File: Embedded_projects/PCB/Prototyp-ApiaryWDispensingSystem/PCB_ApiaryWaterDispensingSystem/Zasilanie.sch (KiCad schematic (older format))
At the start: 17 parts

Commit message: Many design changes have been added over the past few months #3
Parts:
- removed J?: Conn_01x02_Male, symbol Connector:Conn_01x02_Male
- added J6: Conn_02x01, Connector_PinHeader_2.54mm:PinHeader_1x02_P2.54mm_Vertical, symbol Connector_Generic:Conn_02x01
- added J?: Conn_01x02, symbol Connector_Generic:Conn_01x02
- C16, C17: footprint (none) -> Capacitor_Tantalum_SMD:CP_EIA-6032-15_Kemet-U
- C18, C19, C20, C21: footprint (none) -> Capacitor_SMD:C_0603_1608Metric
- D?: footprint (none) -> Diode_SMD:D_SMA
- D?: footprint (none) -> Diode_SMD:D_0603_1608Metric
- JP?: footprint (none) -> Jumper:SolderJumper-2_P1.3mm_Open_TrianglePad1.0x1.5mm
- R28: footprint (none) -> Resistor_SMD:R_0603_1608Metric
- U?: footprint (none) -> Package_SO:SO-8_3.9x4.9mm_P1.27mm
- gave numbers to parts that had none: 1
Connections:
- net +3V3: now also J6.1 (Pin_1)
- net GND: now also C17.2, J?.1 (Pin_1)
- net VDD: now also J6.2 (Pin_2)
- net +VDC renamed VM
- net VM: now also J?.2 (Pin_2)
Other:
- note added: "good"
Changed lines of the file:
@@
 $Descr A4 11693 8268
 encoding utf-8
-Sheet 7 9
+Sheet 6 9
 Title ""
 Date ""
@@
 F 0 "C16" H 1528 2336 50  0000 L CNN
 F 1 "10uF(25V)" H 1528 2245 50  0000 L CNN
-F 2 "" H 1448 2140 50  0001 C CNN
+F 2 "Capacitor_Tantalum_SMD:CP_EIA-6032-15_Kemet-U" H 1448 2140 50  0001 C CNN
 F 3 "~" H 1410 2290 50  0001 C CNN
 	1    1410 2290
@@
 L power:GND #PWR0208
 U 1 1 67F9830C
-P 2930 2510
-F 0 "#PWR0208" H 2930 2260 50  0001 C CNN
-F 1 "GND" H 2935 2337 50  0000 C CNN
-F 2 "" H 2930 2510 50  0001 C CNN
-F 3 "" H 2930 2510 50  0001 C CNN
-	1    2930 2510
+P 2920 2520
+F 0 "#PWR0208" H 2920 2270 50  0001 C CNN
+F 1 "GND" H 2925 2347 50  0000 C CNN
+F 2 "" H 2920 2520 50  0001 C CNN
+F 3 "" H 2920 2520 50  0001 C CNN
+	1    2920 2520
 	1    0    0    -1
 $EndComp
@@
 F 0 "C17" H 3038 2376 50  0000 L CNN
 F 1 "10uF(25V)" H 3038 2285 50  0000 L CNN
-F 2 "" H 2958 2180 50  0001 C CNN
+F 2 "Capacitor_Tantalum_SMD:CP_EIA-6032-15_Kemet-U" H 2958 2180 50  0001 C CNN
 F 3 "~" H 2920 2330 50  0001 C CNN
 	1    2920 2330
@@
 F 0 "D?" H 3100 1843 50  0000 C CNN
 F 1 "D_Small" H 3100 1934 50  0000 C CNN
-F 2 "" V 3100 2050 50  0001 C CNN
+F 2 "Diode_SMD:D_SMA" V 3100 2050 50  0001 C CNN
 F 3 "~" V 3100 2050 50  0001 C CNN
 	1    3100 2050
@@
 $EndComp
 $Comp
-L Connector:Conn_01x03_Male J?
+L Connector:Conn_01x03_Male J5
 U 1 1 67FA01B7
 P 3850 2520
-F 0 "J?" H 3958 2801 50  0000 C CNN
+F 0 "J5" H 3958 2801 50  0000 C CNN
 F 1 "Conn_01x03_Male" H 3900 2140 50  0000 C CNN
 F 2 "Connector_PinHeader_2.54mm:PinHeader_1x03_P2.54mm_Vertical" H 3850 2520 50  0001 C CNN
@@
 	1    0    0    -1
 $EndComp
-Wire Wire Line
-	2920 2180 2920 2150
-Wire Wire Line
-	2920 2150 2630 2150
-Wire Wire Line
-	2920 2150 2920 2050
-Connection ~ 2920 2150
 Connection ~ 2920 2050
 Wire Wire Line
@@
 F 0 "U?" H 3104 3886 50  0000 L CNN
 F 1 "STS7PF30L" H 3104 3795 50  0000 L CNN
-F 2 "" H 2730 3920 50  0001 C CNN
+F 2 "Package_SO:SO-8_3.9x4.9mm_P1.27mm" H 2730 3920 50  0001 C CNN
 F 3 "" H 2730 3920 50  0001 C CNN
 	1    2730 3920
@@
 F 0 "R28" H 2060 4076 50  0000 L CNN
 F 1 "4k7" H 2060 3985 50  0000 L CNN
-F 2 "" V 1920 4030 50  0001 C CNN
+F 2 "Resistor_SMD:R_0603_1608Metric" V 1920 4030 50  0001 C CNN
 F 3 "~" H 1990 4030 50  0001 C CNN
 	1    1990 4030
@@
 F 0 "C20" H 5515 3216 50  0000 L CNN
 F 1 "100n" H 5515 3125 50  0000 L CNN
-F 2 "" H 5438 3020 50  0001 C CNN
+F 2 "Capacitor_SMD:C_0603_1608Metric" H 5438 3020 50  0001 C CNN
 F 3 "~" H 5400 3170 50  0001 C CNN
 	1    5400 3170
@@
 F 0 "C21" H 5095 3066 50  0000 L CNN
 F 1 "1uF_X5R" H 5095 2975 50  0000 L CNN
-F 2 "" H 5018 2870 50  0001 C CNN
+F 2 "Capacitor_SMD:C_0603_1608Metric" H 5018 2870 50  0001 C CNN
 F 3 "~" H 4980 3020 50  0001 C CNN
 	1    4980 3020
@@
 F 0 "C18" H 6915 2996 50  0000 L CNN
 F 1 "1uF_X5R_0603" H 6220 2730 50  0000 L CNN
-F 2 "" H 6838 2800 50  0001 C CNN
+F 2 "Capacitor_SMD:C_0603_1608Metric" H 6838 2800 50  0001 C CNN
 F 3 "~" H 6800 2950 50  0001 C CNN
 	1    6800 2950
@@
 F 0 "C19" H 7315 3196 50  0000 L CNN
 F 1 "100nF" H 7315 3105 50  0000 L CNN
-F 2 "" H 7238 3000 50  0001 C CNN
+F 2 "Capacitor_SMD:C_0603_1608Metric" H 7238 3000 50  0001 C CNN
 F 3 "~" H 7200 3150 50  0001 C CNN
 	1    7200 3150
@@
 F 0 "D?" V 4579 3172 50  0000 R CNN
 F 1 "LED" V 4488 3172 50  0000 R CNN
-F 2 "" H 4540 3290 50  0001 C CNN
+F 2 "Diode_SMD:D_0603_1608Metric" H 4540 3290 50  0001 C CNN
 F 3 "~" H 4540 3290 50  0001 C CNN
 	1    4540 3290
@@
 NoConn ~ 6390 2900
 $Comp
-L Connector:Conn_01x02_Male J?
-U 1 1 67F973BC
-P 8010 2600
-F 0 "J?" H 8118 2781 50  0000 C CNN
-F 1 "Conn_01x02_Male" H 8118 2690 50  0000 C CNN
-F 2 "" H 8010 2600 50  0001 C CNN
-F 3 "~" H 8010 2600 50  0001 C CNN
-	1    8010 2600
-	1    0    0    -1
-$EndComp
-$Comp
 L power:GND #PWR0218
 U 1 1 67F9802C
@@
 	7200 2800 7200 3000
 Connection ~ 6800 2800
-$Comp
-L Jumper:Jumper_2_Open JP?
-U 1 1 67F9CBCE
-P 7600 2800
-F 0 "JP?" H 7470 2920 50  0000 C CNN
-F 1 "Jumper_2_Open" H 7560 2630 50  0000 C CNN
-F 2 "" H 7600 2800 50  0001 C CNN
-F 3 "~" H 7600 2800 50  0001 C CNN
-	1    7600 2800
-	1    0    0    -1
-$EndComp
 Wire Wire Line
 	7400 2800 7200 2800
@@
 Wire Wire Line
 	7800 2800 7870 2800
-Wire Wire Line
-	8250 2800 8250 2700
-Wire Wire Line
-	8250 2700 8210 2700
 $Comp
 L power:+3.3V #PWR0219
@@
 	7870 2760 7870 2800
 Connection ~ 7870 2800
-Wire Wire Line
-	7870 2800 8250 2800
-$Comp
-L power:VDD #PWR?
+$Comp
+L power:VDD #PWR0238
 U 1 1 6830AB4B
-P 8580 2510
-F 0 "#PWR?" H 8580 2360 50  0001 C CNN
-F 1 "VDD" H 8595 2683 50  0000 C CNN
-F 2 "" H 8580 2510 50  0001 C CNN
-F 3 "" H 8580 2510 50  0001 C CNN
-	1    8580 2510
-	1    0    0    -1
-$EndComp
-Wire Wire Line
-	8210 2600 8580 2600
-Wire Wire Line
-	8580 2600 8580 2510
-$Comp
-L power:+5VP #PWR?
+P 8955 2800
+F 0 "#PWR0238" H 8955 2650 50  0001 C CNN
+F 1 "VDD" H 8970 2973 50  0000 C CNN
+F 2 "" H 8955 2800 50  0001 C CNN
+F 3 "" H 8955 2800 50  0001 C CNN
+	1    8955 2800
+	1    0    0    -1
+$EndComp
+$Comp
+L power:+5VP #PWR0239
 U 1 1 68379F03
 P 1800 3620
-F 0 "#PWR?" H 1800 3470 50  0001 C CNN
+F 0 "#PWR0239" H 1800 3470 50  0001 C CNN
 F 1 "+5VP" H 1815 3793 50  0000 C CNN
 F 2 "" H 1800 3620 50  0001 C CNN
@@
 Wire Wire Line
 	2230 2350 2230 2650
-$Comp
-L power:+VDC #PWR?
-U 1 1 689704B4
-P 1000 1780
-F 0 "#PWR?" H 1000 1680 50  0001 C CNN
-F 1 "+VDC" H 1000 2055 50  0000 C CNN
-F 2 "" H 1000 1780 50  0001 C CNN
-F 3 "" H 1000 1780 50  0001 C CNN
-	1    1000 1780
-	1    0    0    -1
-$EndComp
-Wire Wire Line
-	1000 1780 1000 2050
+Wire Wire Line
+	2920 2050 2920 2180
+Wire Wire Line
+	2920 2480 2920 2520
+Text HLabel 1115 920  0    50   Output ~ 0
+PWR_ENn
+Text GLabel 1285 920  2    50   Output ~ 0
+PWR_ENn
+Wire Wire Line
+	1285 920  1115 920
+Text Notes 925  2375 0    50   ~ 0
+good
+$Comp
+L Jumper:Jumper_2_Open JP?
+U 1 1 67F9CBCE
+P 7600 2800
+F 0 "JP?" H 7470 2920 50  0000 C CNN
+F 1 "Jumper_2_Open" H 7560 2630 50  0000 C CNN
+F 2 "Jumper:SolderJumper-2_P1.3mm_Open_TrianglePad1.0x1.5mm" H 7600 2800 50  0001 C CNN
+F 3 "~" H 7600 2800 50  0001 C CNN
+	1    7600 2800
+	1    0    0    -1
+$EndComp
+$Comp
+L Connector_Generic:Conn_02x01 J6
+U 1 1 68EED7C1
+P 8520 2800
+F 0 "J6" H 8570 3017 50  0000 C CNN
+F 1 "Conn_02x01" H 8570 2926 50  0000 C CNN
+F 2 "Connector_PinHeader_2.54mm:PinHeader_1x02_P2.54mm_Vertical" H 8520 2800 50  0001 C CNN
+F 3 "~" H 8520 2800 50  0001 C CNN
+	1    8520 2800
+	1    0    0    -1
+$EndComp
+Wire Wire Line
+	7870 2800 8320 2800
+Wire Wire Line
+	8955 2800 8820 2800
+$Comp
+L Connector_Generic:Conn_01x02 J?
+U 1 1 68ED6183
+P 640 2150
+F 0 "J?" H 558 1825 50  0000 C CNN
+F 1 "Conn_01x02" H 558 1916 50  0000 C CNN
+F 2 "" H 640 2150 50  0001 C CNN
+F 3 "~" H 640 2150 50  0001 C CNN
+	1    640  2150
+	-1   0    0    1
+$EndComp
+Wire Wire Line
+	1000 2050 840  2050
+Connection ~ 1000 2050
+$Comp
+L power:GND #PWR?
+U 1 1 68ED818B
+P 895 2150
+F 0 "#PWR?" H 895 1900 50  0001 C CNN
+F 1 "GND" H 900 1977 50  0000 C CNN
+F 2 "" H 895 2150 50  0001 C CNN
+F 3 "" H 895 2150 50  0001 C CNN
+	1    895  2150
+	1    0    0    -1
+$EndComp
+Wire Wire Line
+	895  2150 840  2150
+Text GLabel 1285 1050 2    50   Output ~ 0
+VM
+Text HLabel 1115 1050 0    50   Output ~ 0
+VM
+Wire Wire Line
+	1285 1050 1115 1050
+Text GLabel 915  1755 0    50   Output ~ 0
+VM
+Wire Wire Line
+	915  1755 1000 1755
+Wire Wire Line
+	1000 1755 1000 2050
 $EndSCHEMATC

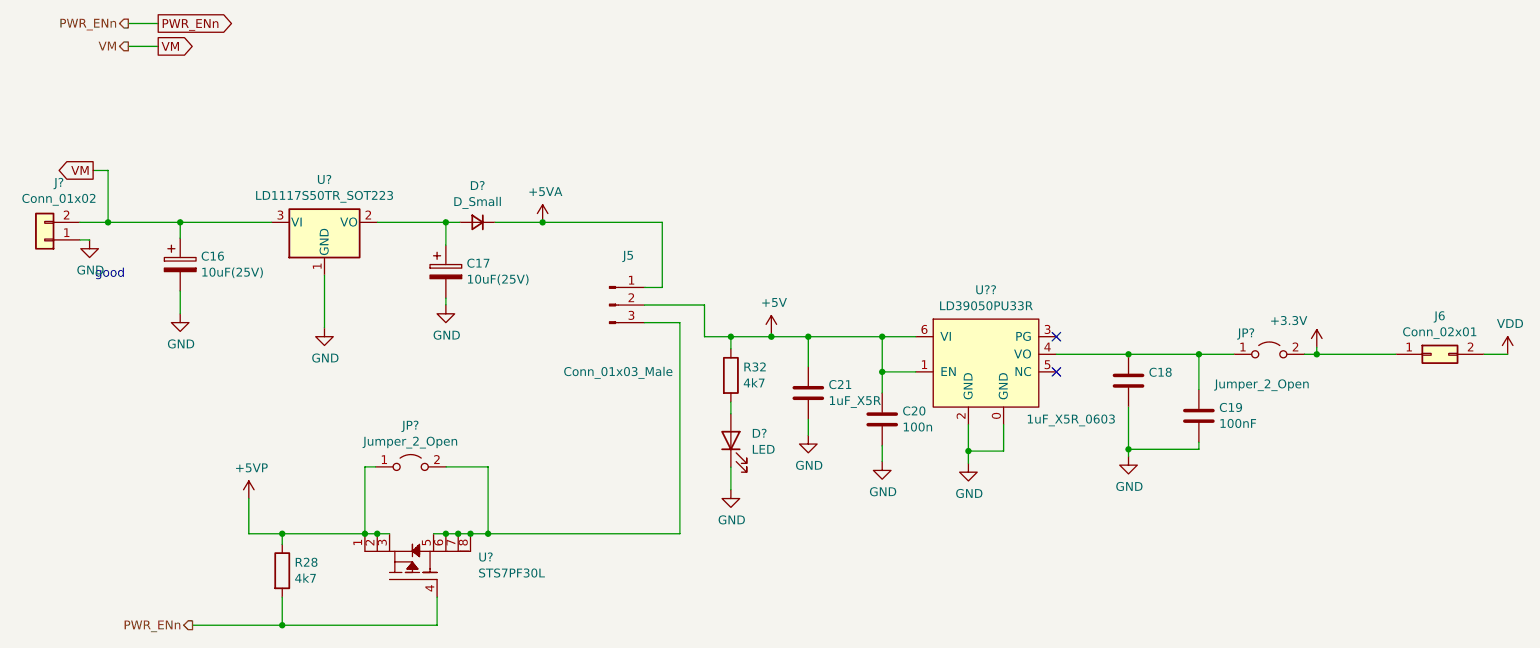
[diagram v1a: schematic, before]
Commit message: All signal has been routed, the analog part needs to be completed
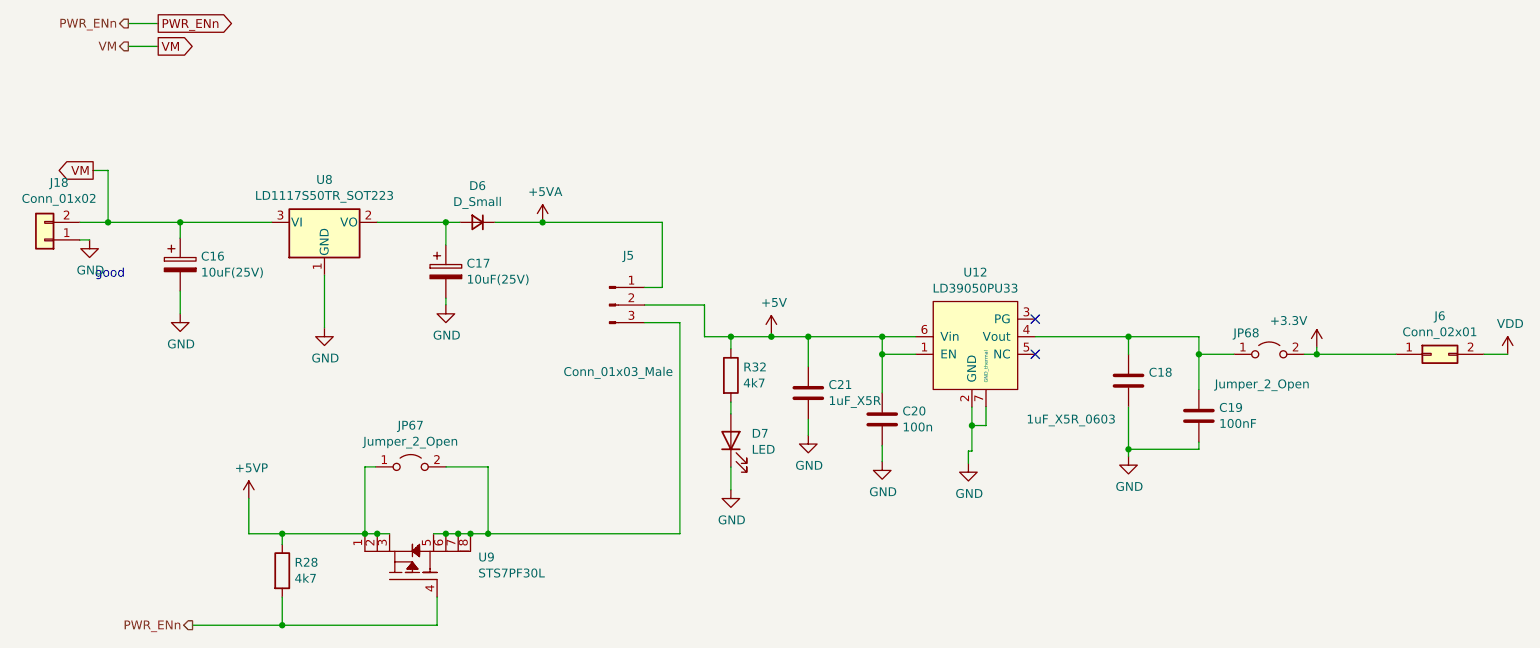
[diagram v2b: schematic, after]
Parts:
- removed U??: LD39050PU33R, symbol ApiaryWaterDispensingSystem:LD39050PU33R
- added U12: LD39050PU33, Package_SON:WSON-6-1EP_3x3mm_P0.95mm, symbol ApiaryWaterDispensingSystem:LD39050PU33
- J18: renamed from J?; footprint (none) -> TerminalBlock_4Ucon:TerminalBlock_4Ucon_1x02_P3.50mm_Vertical
- JP67: renamed from JP?; footprint (none) -> Jumper:SolderJumper-2_P1.3mm_Open_TrianglePad1.0x1.5mm
- R32: footprint (none) -> Resistor_SMD:R_0603_1608Metric
- gave numbers to parts that had none: 5
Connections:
- net +5V: now also U12.1 (EN), U12.6 (Vin)
- net GND: now also U12.2 (GND), U12.7 (GND_thermal)
- net at C18.1, C19.1, JP68.1 (A): now also U12.4 (Vout)
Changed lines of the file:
@@
 $EndDescr
-$Comp
-L ApiaryWaterDispensingSystem:LD39050PU33R U??
-U 1 1 67F96C5D
-P 5990 2800
-F 0 "U??" H 5990 3165 50  0000 C CNN
-F 1 "LD39050PU33R" H 5990 3074 50  0000 C CNN
-F 2 "" H 5990 2800 50  0001 C CNN
-F 3 "" H 5990 2800 50  0001 C CNN
-	1    5990 2800
-	1    0    0    -1
-$EndComp
 $Comp
 L Device:CP C16
@@
 $EndComp
 $Comp
-L Device:D_Small D?
+L Device:D_Small D6
 U 1 1 67F9ACDF
 P 3100 2050
-F 0 "D?" H 3100 1843 50  0000 C CNN
+F 0 "D6" H 3100 1843 50  0000 C CNN
 F 1 "D_Small" H 3100 1934 50  0000 C CNN
 F 2 "Diode_SMD:D_SMA" V 3100 2050 50  0001 C CNN
@@
 Connection ~ 4770 2700
 $Comp
-L Jumper:Jumper_2_Open JP?
+L Jumper:Jumper_2_Open JP67
 U 1 1 67FA53C3
 P 2720 3440
-F 0 "JP?" H 2720 3675 50  0000 C CNN
+F 0 "JP67" H 2720 3675 50  0000 C CNN
 F 1 "Jumper_2_Open" H 2720 3584 50  0000 C CNN
-F 2 "" H 2720 3440 50  0001 C CNN
+F 2 "Jumper:SolderJumper-2_P1.3mm_Open_TrianglePad1.0x1.5mm" H 2720 3440 50  0001 C CNN
 F 3 "~" H 2720 3440 50  0001 C CNN
 	1    2720 3440
@@
 $EndComp
 $Comp
-L ApiaryWaterDispensingSystem:STS7PF30L U?
+L ApiaryWaterDispensingSystem:STS7PF30L U9
 U 1 1 67FAB112
 P 2730 3920
-F 0 "U?" H 3104 3886 50  0000 L CNN
+F 0 "U9" H 3104 3886 50  0000 L CNN
 F 1 "STS7PF30L" H 3104 3795 50  0000 L CNN
 F 2 "Package_SO:SO-8_3.9x4.9mm_P1.27mm" H 2730 3920 50  0001 C CNN
@@
 F 0 "R32" H 4610 2966 50  0000 L CNN
 F 1 "4k7" H 4610 2875 50  0000 L CNN
-F 2 "" V 4470 2920 50  0001 C CNN
+F 2 "Resistor_SMD:R_0603_1608Metric" V 4470 2920 50  0001 C CNN
 F 3 "~" H 4540 2920 50  0001 C CNN
 	1    4540 2920
@@
 $EndComp
 $Comp
-L Device:LED D?
+L Device:LED D7
 U 1 1 67FB2F5D
 P 4540 3290
-F 0 "D?" V 4579 3172 50  0000 R CNN
+F 0 "D7" V 4579 3172 50  0000 R CNN
 F 1 "LED" V 4488 3172 50  0000 R CNN
 F 2 "Diode_SMD:D_0603_1608Metric" H 4540 3290 50  0001 C CNN
@@
 Wire Wire Line
 	5400 3410 5400 3320
-Wire Wire Line
-	5590 2900 5400 2900
-Wire Wire Line
-	5400 2900 5400 3020
-Wire Wire Line
-	5400 2900 5400 2700
-Connection ~ 5400 2900
 Connection ~ 5400 2700
 Wire Wire Line
@@
 $EndComp
 Wire Wire Line
-	6090 3200 6090 3350
-Wire Wire Line
-	6090 3350 5890 3350
-Wire Wire Line
-	5890 3350 5890 3200
-Wire Wire Line
 	5890 3350 5890 3420
-Connection ~ 5890 3350
 Wire Wire Line
 	2600 3820 2530 3820
@@
 	1990 4340 1480 4340
 Connection ~ 1990 4340
-NoConn ~ 6390 2700
-NoConn ~ 6390 2900
 $Comp
 L power:GND #PWR0218
@@
 Connection ~ 6800 3340
 Wire Wire Line
-	6390 2800 6800 2800
-Wire Wire Line
-	6800 2800 7200 2800
-Wire Wire Line
 	7200 2800 7200 3000
-Connection ~ 6800 2800
 Wire Wire Line
 	7400 2800 7200 2800
-Connection ~ 7200 2800
 Wire Wire Line
 	7800 2800 7870 2800
@@
 	1800 3620 1800 3820
 $Comp
-L Regulator_Linear:LD1117S50TR_SOT223 U?
+L Regulator_Linear:LD1117S50TR_SOT223 U8
 U 1 1 68332228
 P 2230 2050
-F 0 "U?" H 2230 2292 50  0000 C CNN
+F 0 "U8" H 2230 2292 50  0000 C CNN
 F 1 "LD1117S50TR_SOT223" H 2230 2201 50  0000 C CNN
 F 2 "Package_TO_SOT_SMD:SOT-223-3_TabPin2" H 2230 2250 50  0001 C CNN
@@
 good
 $Comp
-L Jumper:Jumper_2_Open JP?
+L Jumper:Jumper_2_Open JP68
 U 1 1 67F9CBCE
 P 7600 2800
-F 0 "JP?" H 7470 2920 50  0000 C CNN
+F 0 "JP68" H 7470 2920 50  0000 C CNN
 F 1 "Jumper_2_Open" H 7560 2630 50  0000 C CNN
 F 2 "Jumper:SolderJumper-2_P1.3mm_Open_TrianglePad1.0x1.5mm" H 7600 2800 50  0001 C CNN
@@
 	8955 2800 8820 2800
 $Comp
-L Connector_Generic:Conn_01x02 J?
+L Connector_Generic:Conn_01x02 J18
 U 1 1 68ED6183
 P 640 2150
-F 0 "J?" H 558 1825 50  0000 C CNN
+F 0 "J18" H 558 1825 50  0000 C CNN
 F 1 "Conn_01x02" H 558 1916 50  0000 C CNN
-F 2 "" H 640 2150 50  0001 C CNN
+F 2 "TerminalBlock_4Ucon:TerminalBlock_4Ucon_1x02_P3.50mm_Vertical" H 640 2150 50  0001 C CNN
 F 3 "~" H 640 2150 50  0001 C CNN
 	1    640  2150
@@
 Connection ~ 1000 2050
 $Comp
-L power:GND #PWR?
+L power:GND #PWR027
 U 1 1 68ED818B
 P 895 2150
-F 0 "#PWR?" H 895 1900 50  0001 C CNN
+F 0 "#PWR027" H 895 1900 50  0001 C CNN
 F 1 "GND" H 900 1977 50  0000 C CNN
 F 2 "" H 895 2150 50  0001 C CNN
@@
 Wire Wire Line
 	1000 1755 1000 2050
+$Comp
+L ApiaryWaterDispensingSystem:LD39050PU33 U12
+U 1 1 69136F8C
+P 5910 2700
+F 0 "U12" H 5930 3065 50  0000 C CNN
+F 1 "LD39050PU33" H 5930 2974 50  0000 C CNN
+F 2 "Package_SON:WSON-6-1EP_3x3mm_P0.95mm" H 5910 2700 50  0001 C CNN
+F 3 "" H 5910 2700 50  0001 C CNN
+	1    5910 2700
+	1    0    0    -1
+$EndComp
+Wire Wire Line
+	6270 2700 6800 2700
+Wire Wire Line
+	6800 2700 6800 2800
+Wire Wire Line
+	6800 2700 7200 2700
+Wire Wire Line
+	7200 2700 7200 2800
+Connection ~ 6800 2700
+Connection ~ 7200 2800
+NoConn ~ 6270 2600
+NoConn ~ 6270 2800
+Wire Wire Line
+	5400 2700 5400 2800
+Wire Wire Line
+	5590 2800 5400 2800
+Connection ~ 5400 2800
+Wire Wire Line
+	5400 2800 5400 3020
+Wire Wire Line
+	5910 3100 5910 3205
+Wire Wire Line
+	5910 3350 5890 3350
+Wire Wire Line
+	5990 3100 5990 3205
+Wire Wire Line
+	5990 3205 5910 3205
+Connection ~ 5910 3205
+Wire Wire Line
+	5910 3205 5910 3350
 $EndSCHEMATC
